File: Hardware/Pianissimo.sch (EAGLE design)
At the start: 65 parts, among them U1 LM386N

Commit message: which note corresponds to which circuit
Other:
- note added: "Note: C5"
- note added: "Note: D5"
- note added: "Note: E5"
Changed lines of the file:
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@@
 <text x="142.24" y="73.66" size="1.778" layer="91">Exact resistor value is 624819Ohms</text>
 <text x="327.66" y="76.2" size="1.778" layer="91">Capacitor is optional</text>
+<text x="116.84" y="106.68" size="3.81" layer="91">Note: C5</text>
+<text x="116.84" y="43.18" size="3.81" layer="91">Note: D5</text>
+<text x="116.84" y="-20.32" size="3.81" layer="91">Note: E5</text>
 </plain>
 <instances>

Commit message: more updates
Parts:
- removed C22, C23: 100n, CalvEngIO-Passives:CAPACITOR0402
- removed C24: 33n, CalvEngIO-Passives:CAPACITOR0402
- removed C25: 100p, CalvEngIO-Passives:CAPACITOR0402
- removed C26: (no value), CalvEngIO-Passives:CAPACITOR.POLARC-EEU-FM-A-220UF
- removed C27: (no value), CalvEngIO-Passives:CAPACITOR0603
- removed R35: 10k, CalvEngIO-Passives:RESISTOR0402-SMALLER
- removed R37, R38, R39, R40: 556k, CalvEngIO-Passives:RESISTOR0402-SMALLER
- removed R47: 39k, CalvEngIO-Passives:RESISTOR0402-SMALLER
- removed R48: 270k, CalvEngIO-Passives:RESISTOR0402-SMALLER
- removed R49: (no value), CalvEngIO-Passives:R-TRIMM5W
- removed R50: (no value), CalvEngIO-Passives:RESISTOR0603
- removed U$16, U$19, U$24, U$27, U$29, U$3, U$4, U$5, U$6, U$7: 741.OP, CalvEngIO-AnalogIC:741.OP
- added C16, C17, C19: 10n, CalvEngIO-Passives:CAPACITOR0402
- added C7: 100n, CalvEngIO-Passives:CAPACITOR0402
- added C8: 50n, CalvEngIO-Passives:CAPACITOR0603
- added C9: 250u, CalvEngIO-Passives:CAPACITOR.POLARC-EEU-FM-A-220UF
- added LOGO1: OSHW-LOGOL, CalvEngIO-Logos:OSHW-LOGOL
- added OP1, OP2, OP3, OP4, OP5: (no value), CalvEngIO-AnalogIC:OP-DUALR
- added R10, R14, R15: 10k, CalvEngIO-Passives:RESISTOR0402-SMALLER
- added R17: 625k, CalvEngIO-Passives:RESISTOR0402-SMALLER
- added R18: 701k, CalvEngIO-Passives:RESISTOR0402-SMALLER
- added R26, R29, R32: 30k, CalvEngIO-Passives:RESISTOR0402-SMALLER
- added R27, R30, R33: 27k, CalvEngIO-Passives:RESISTOR0402-SMALLER
- added R28, R31: 24k, CalvEngIO-Passives:RESISTOR0402-SMALLER
- added R9: 39k, CalvEngIO-Passives:RESISTOR0402-SMALLER
- added REV1: REVISION.A, CalvEngIO-Symbols:REVISION.A
- C10, C12, C13, C14, C15, C18, C20, C21: value 100n -> 10n
- C11: value 33n -> 10n
- C2, C3: value 100n -> 33n
- C4: value 100n -> 3.3n
- R1, R2, R3, R4: value 625k -> 10k
- R11: value 39k -> 10k
- R12: value (none) -> 39k
- R13: value (none) -> 10k
- R21: value 701k -> 10k
- R22: value 701k -> 10; device CalvEngIO-Passives:RESISTOR0402-SMALLER -> CalvEngIO-Passives:RESISTOR0603
- R23: value 701k -> 30k
- R24: value 701k -> 27k
- R25: value 701k -> 24k
- R34: value 10k -> 24k
- R7: value 625k -> 39k
- renumbered R36 to R16
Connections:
- removed net N$54: R49.S, U1.+IN
- removed net NOTE_1: R11.2, SW1.B
- removed net NOTE_2: R8.2, SW2.B
- removed net NOTE_3: R47.2, SW3.B
- removed net V-: U$16G$2.V-, U$24G$2.V-, U$3G$2.V-, U$5G$2.V-, U$7G$2.V-
- new net 5V: OP2P.V+, OP3P.V+, R1.2, R10.1, R3.2, R5.2, U1.V+
- new net C5: R8.2, SW1.B, SW2.B
- new net CF: R7.2
- new net E5: R9.2, SW3.B
- new net N$13: C5.1, OP1B.-IN, OP1B.OUT, R13.1
- new net N$17: C6.1, OP2B.-IN, OP2B.OUT, R14.1
- new net N$19: C7.1, OP3B.-IN, OP3B.OUT, R15.1
- new net N$21: OP1B.+IN, R1.1, R2.2
- new net N$29: OP2B.+IN, R3.1, R4.2
- new net N$30: OP3B.+IN, R5.1, R6.2
- net GND: now also C10.2, C11.2, C16.2, C17.2, C18.2, C19.2, OP1P.V-, OP2P.V-, OP3P.V-, R11.2, R2.1, R22.1, R4.1; no longer C10.1, C18.1, C2.2, C22.2, C23.2, C3.2, C4.1, C5.2, C6.2, R12.2, R20.1, R35.1, R49.A, R50.1
- net N$1: now also OP2A.OUT, R17.1, R20.2, R24.1; no longer R1.1, R5.2, R7.1, U$3G$1.OUT
- net N$10: now also C2.1; no longer C1.1
- net N$11: now also OP4A.-IN, OP4A.OUT; no longer U$27G$1.-IN, U$27G$1.OUT
- net N$14: now also OP5A.-IN, OP5A.OUT; no longer U$19G$1.-IN, U$19G$1.OUT
- net N$16: now also OP4B.-IN, OP4B.OUT; no longer U$4G$1.-IN, U$4G$1.OUT
- net N$2: now also OP2A.+IN, R14.2, R20.1; no longer R5.1, R6.2, U$3G$1.+IN
- net N$22: now also OP3A.OUT, R18.1, R21.2, R25.1; no longer R19.2, R21.1, R22.1, U$16G$1.OUT
- net N$23: now also OP3A.+IN, R15.2, R21.1; no longer R19.1, R20.2, U$16G$1.+IN
- net N$24: now also C7.2, OP3A.-IN, R18.2; no longer C10.2, R21.2, U$16G$1.-IN
- net N$25: now also R25.2, R28.1; no longer R22.2, R23.1
- net N$26: now also C15.1, R28.2, R31.1; no longer C13.1, R23.2, R24.1
- net N$27: now also C18.1, R31.2, R34.1; no longer C14.1, R24.2, R25.1
- net N$28: now also C21.1, OP5A.+IN, R34.2; no longer C15.1, R25.2, U$19G$1.+IN
- net N$3: now also C6.2, OP2A.-IN, R17.2; no longer C4.2, R7.2, U$3G$1.-IN
- net N$38: now also OP1A.OUT, R19.2, R23.1; no longer R34.2, R37.1, U$24G$1.OUT
- net N$39: now also OP1A.+IN, R13.2, R19.1; no longer R34.1, R35.2, U$24G$1.+IN
- net N$4: now also C11.1, R24.2, R27.1; no longer C2.1, R1.2, R2.1
- net N$40: now also C5.2, OP1A.-IN; no longer C18.2, U$24G$1.-IN
- net N$41: now also C10.1, R23.2, R26.1; no longer C20.1, R37.2, R38.1
- net N$42: now also C13.1, R26.2, R29.1; no longer C21.1, R38.2, R39.1
- net N$43: now also C16.1, R29.2, R32.1; no longer C22.1, R39.2, R40.1
- net N$44: now also C19.1, OP4A.+IN, R32.2; no longer C23.1, R40.2, U$27G$1.+IN
- net N$5: now also C14.1, R27.2, R30.1; no longer C3.1, R2.2, R3.1
- net N$50: now also C3.1, R9.1; no longer C24.1, R47.1
- net N$51: now also C2.2, C3.2, C4.1, OP5B.-IN, R12.2; no longer C11.2, C24.2, C25.1, R48.2, U$29G$1.-IN
- net N$55: now also C4.2, OP5B.OUT, R12.1, U1.+IN; no longer C25.2, R48.1, R49.E, U$29G$1.OUT
- net N$56: now also C8.1, C9.+; no longer C26.+, C27.1
- net N$57: now also C9.-; no longer C26.-
- net N$58: now also C8.2, R22.2; no longer C27.2, R50.2
- net N$6: now also C17.1, R30.2, R33.1; no longer C5.1, R3.2, R4.1
- net N$7: now also C20.1, OP4B.+IN, R33.2; no longer C6.1, R4.2, U$4G$1.+IN
- net N$8: now also OP5B.+IN, R10.2, R11.1; no longer R12.1, R13.2, U$29G$1.+IN
- net N$9: now also C1.1, R7.1; no longer C11.1, R11.1
- net V+: now also OP1P.V+; no longer R13.1, U$16G$2.V+, U$24G$2.V+, U$3G$2.V+, U$5G$2.V+, U$7G$2.V+, U1.V+
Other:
- note added: "#FunTimesWithTheTA"
- note added: "By: Orlando Hoilett"
- note added: "PIANISSIMO"
- note added: "Square Wave to Sine Wave Converter using a 4-Pole Low-Pass Filter fc = 530Hz"
- note added: "Square Wave to Sine Wave Converter using a 4-Pole Low-Pass Filter fc = 589Hz"
- note added: "Square Wave to Sine Wave Converter using a 4-Pole Low-Pass Filter fc = 663Hz"
- note added: "f = 523.2511"
- note added: "f = 587.3295"
- note added: "f = 659.2551"
- note added: "fc = 1.2kHz"
- note added: "fc = 120Hz"
- note removed: "Capacitor is optional"
- note removed: "Exact resistor value is 556383Ohms"
- note removed: "Exact resistor value is 624819Ohms"
- note removed: "Square Wave to Sine Wave Converter using a 4-Pole Low-Pass Filter"
- moved on the sheet: C1, C10, C11, C12, C13, C14, C15, C18, C2, C20, C21, C3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

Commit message: updates and ready to roll
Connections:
- removed net CF: R7.2
- new net D5: R8.2, SW2.B
- net C5: now also R7.2; no longer R8.2, SW2.B
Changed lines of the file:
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@@
 <pinref part="SW3" gate="G$1" pin="B"/>
 <wire x1="251.46" y1="2.54" x2="254" y2="2.54" width="0.1524" layer="91"/>
-<label x="254" y="2.54" size="1.27" layer="95" xref="yes"/>
+<label x="254" y="2.54" size="1.778" layer="95" xref="yes"/>
 </segment>
 </net>
@@
 <junction x="208.28" y="129.54"/>
 <pinref part="OP4" gate="A" pin="+IN"/>
-</segment>
-</net>
-<net name="CF" class="0">
-<segment>
-<pinref part="R7" gate="G$1" pin="2"/>
-<wire x1="60.96" y1="-50.8" x2="55.88" y2="-50.8" width="0.1524" layer="91"/>
-<label x="55.88" y="-50.8" size="1.778" layer="95" rot="R180" xref="yes"/>
 </segment>
 </net>
@@
 <pinref part="SW1" gate="G$1" pin="B"/>
 <wire x1="251.46" y1="127" x2="254" y2="127" width="0.1524" layer="91"/>
-<label x="254" y="127" size="1.27" layer="95" xref="yes"/>
+<label x="254" y="127" size="1.778" layer="95" xref="yes"/>
+</segment>
+<segment>
+<pinref part="R7" gate="G$1" pin="2"/>
+<wire x1="60.96" y1="-50.8" x2="55.88" y2="-50.8" width="0.1524" layer="91"/>
+<label x="55.88" y="-50.8" size="1.778" layer="95" rot="R180" xref="yes"/>
+</segment>
+</net>
+<net name="D5" class="0">
+<segment>
+<pinref part="SW2" gate="G$1" pin="B"/>
+<wire x1="251.46" y1="63.5" x2="254" y2="63.5" width="0.1524" layer="91"/>
+<label x="254" y="63.5" size="1.778" layer="95" xref="yes"/>
 </segment>
 <segment>
@@
 <label x="55.88" y="-63.5" size="1.778" layer="95" rot="R180" xref="yes"/>
 </segment>
-<segment>
-<pinref part="SW2" gate="G$1" pin="B"/>
-<wire x1="251.46" y1="63.5" x2="254" y2="63.5" width="0.1524" layer="91"/>
-<label x="254" y="63.5" size="1.27" layer="95" xref="yes"/>
-</segment>
-</net>
+</net>

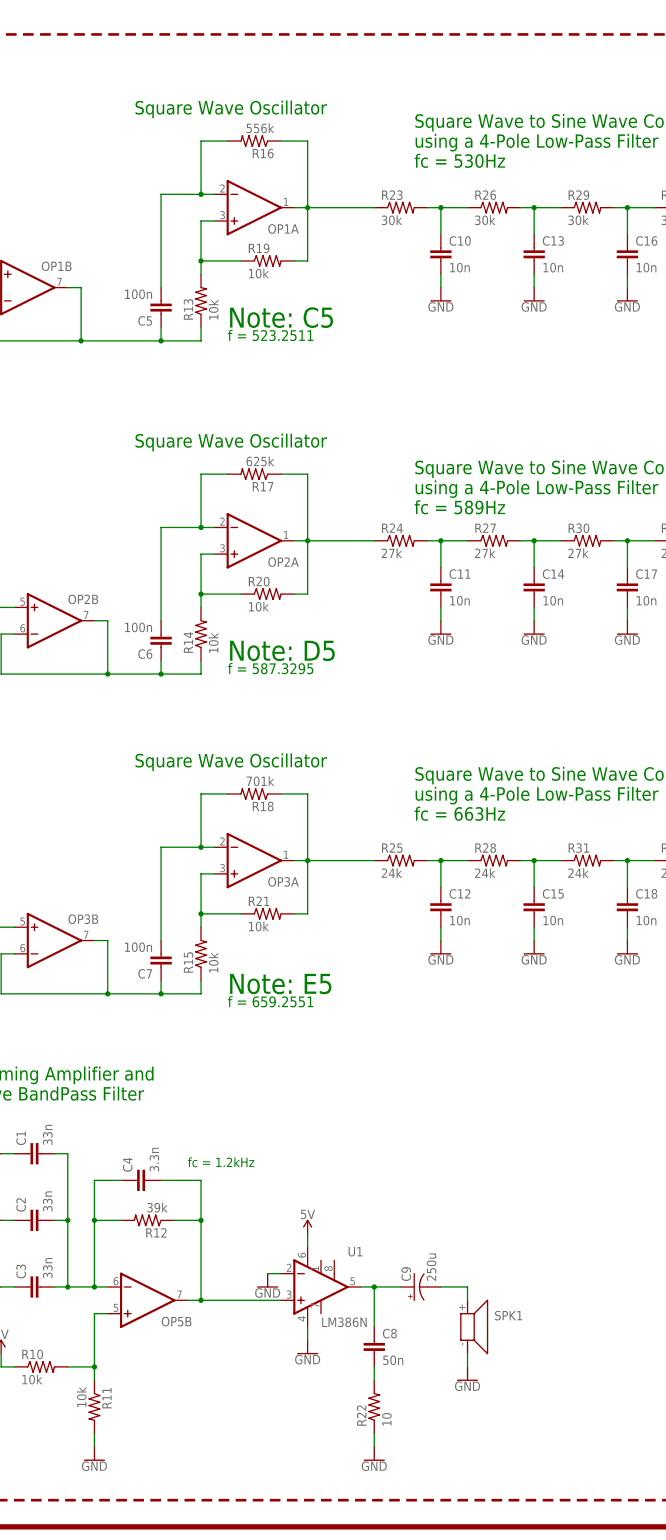
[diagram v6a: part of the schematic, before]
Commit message: updates to match correct resistor values for oscillator circuits
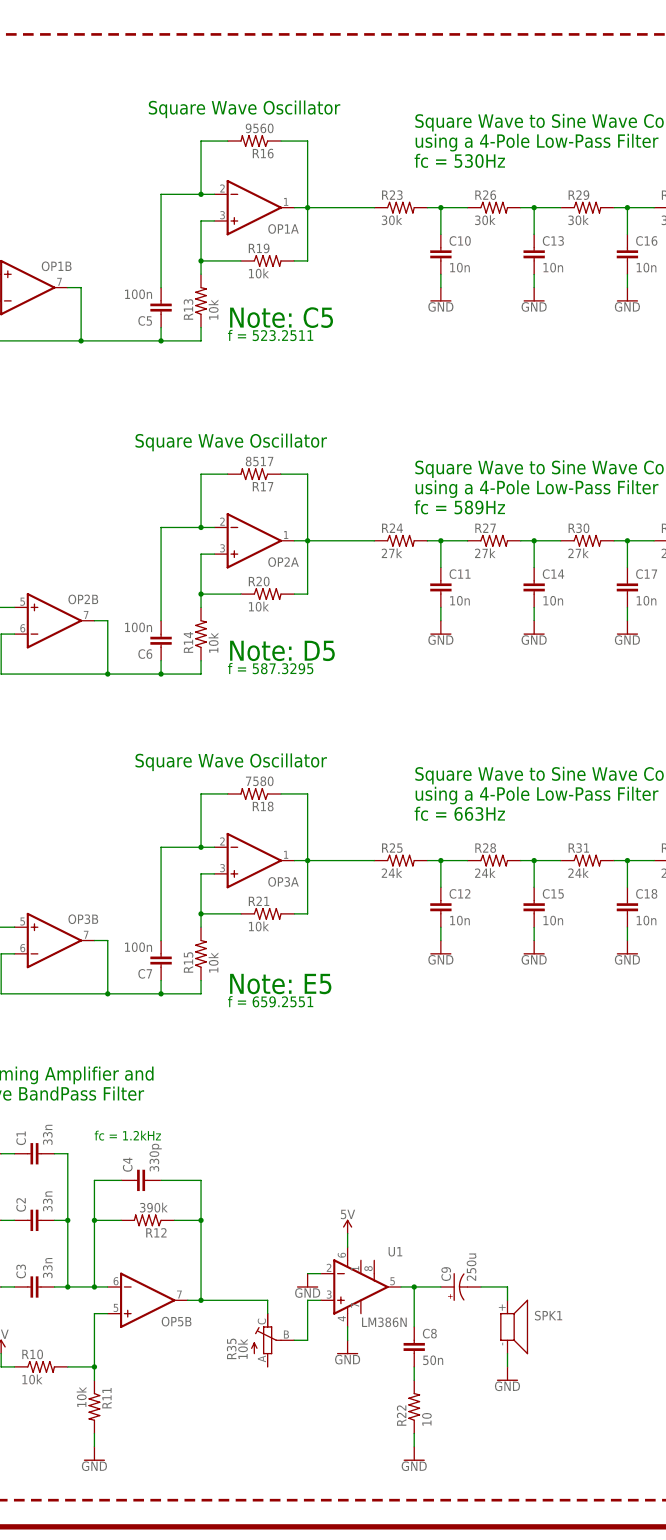
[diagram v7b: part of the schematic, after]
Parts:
- added R35: 10k, CalvEngIO-Passives:R-TRIMM-CB10V
- C4: value 3.3n -> 330p
- R12: value 39k -> 390k
- R16: value 556k -> 9560
- R17: value 625k -> 8517
- R18: value 701k -> 7580
- REV1: value REVISION.A -> REVISION.B; device CalvEngIO-Symbols:REVISION.A -> CalvEngIO-Symbols:REVISION.B
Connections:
- new net N$12: R35.S, U1.+IN
- net N$55: now also R35.E; no longer U1.+IN
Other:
- moved on the sheet: C8, C9, R22, SPK1, U1
